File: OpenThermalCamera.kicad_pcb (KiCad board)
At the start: 2 copper layers, 26 x 20 mm, 18 parts, among them J1 Conn_ARM_JTAG_SWD_10, J2 USB_CONN, SW1 PB_Bootloader, U1 MLX90640, U2 TPS793333-EP, U3 STM32F042F6Px, U4 NUP2202

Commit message: Rev2
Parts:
- added D1: LED_Dual_ACAC, LED_SMD:LED_Cree-PLCC4_2x2mm_CW, B.Cu at (31.0, 30.7)
- added G1: , Symbol:OSHW-Logo2_7.3x6mm_SilkScreen, F.Cu at (31.2, 43.4)
- added R4: 5k1, Resistor_SMD:R_0805_2012Metric_Pad1.15x1.40mm_HandSolder, B.Cu at (34.4, 33.2)
- added R5: 10R, Resistor_SMD:R_0805_2012Metric_Pad1.15x1.40mm_HandSolder, F.Cu at (36.7, 43.9)
- added R6: 130R, Resistor_SMD:R_0805_2012Metric_Pad1.15x1.40mm_HandSolder, F.Cu at (36.7, 42.0)
- J2: value USB_CONN -> DX07P024AJ1R1500; footprint usb_b2b_connector:usb_b2b_connector -> lib_fp:DX07P024AJ1R1500
- R2, R3: value 2k2 -> 4k7
- SW1: footprint Button_Switch_SMD:SW_SPST_FSMSM -> Jumper:SolderJumper-2_P1.3mm_Open_RoundedPad1.0x1.5mm
- U1: footprint Package_TO_SOT_THT:TO-39-4_Window -> lib_fp:MLX90640
- moved SW1 20.3 mm to (49.7, 44.3)
- moved J2 4.70 mm to (40.4, 29.5), turned to 180 degrees
- moved U4 4.25 mm to (46.2, 33.4)
- moved R3 3.81 mm to (40.2, 36.6)
- moved C2 1.60 mm to (44.4, 43.7)
- moved U2 1.10 mm to (46.8, 43.6)
- moved C5 0.90 mm to (33.1, 36.7)
- moved C1 0.80 mm to (49.4, 43.7)
- moved C4 0.71 mm to (35.5, 36.6)
- moved C3 0.70 mm to (46.8, 40.2)
- moved C6 0.60 mm to (51.3, 43.7)
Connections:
- U3 pad 17: /USB_P -> /USB_N
- U3 pad 18: /USB_N -> /USB_P
- U3 pad 6: Net-(U3-Pad6) -> /BLUE_LED
- U3 pad 7: Net-(U3-Pad7) -> /RED_LED
- U4 pad 1: /USB_N -> /USB_P
- U4 pad 6: /USB_P -> /USB_N
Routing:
- net /BOOT0: track 39.2 -> 6.43 mm
- net Net-(D1-Pad1): track 0.00 -> 17.4 mm, vias 0 -> 1
- net Net-(D1-Pad4): track 0.00 -> 14.7 mm, vias 0 -> 1
- net +5V: track 33.2 -> 46.0 mm, vias 0 -> 3
- net Net-(J2-PadA5): track 0.00 -> 10.3 mm, vias 0 -> 1
- net /BLUE_LED: track 0.00 -> 8.67 mm, vias 0 -> 1
- net /RED_LED: track 0.00 -> 8.16 mm, vias 0 -> 1
- net GND: track 91.9 -> 84.6 mm, vias 11 -> 12
- net +3V3: track 62.5 -> 56.2 mm
- net /USB_P: track 32.5 -> 26.5 mm
- net /USB_N: track 31.4 -> 27.9 mm
- net /I2C_SDA: track 13.3 -> 12.3 mm, vias 2 -> 1
- net /I2C_SCL: track 8.79 -> 9.21 mm, vias 2 -> 1
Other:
- board size 26 x 20 mm -> 26 x 20.6 mm
- board text added: "OTC Rev2"

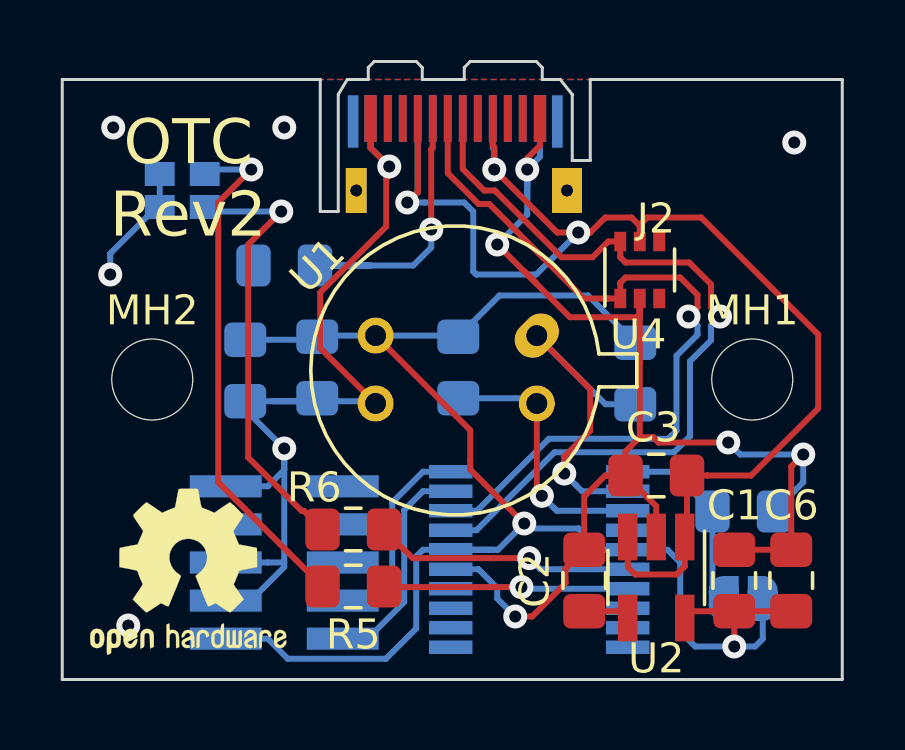
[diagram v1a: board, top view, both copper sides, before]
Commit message: Rev3: fixed MLX90640 footprint
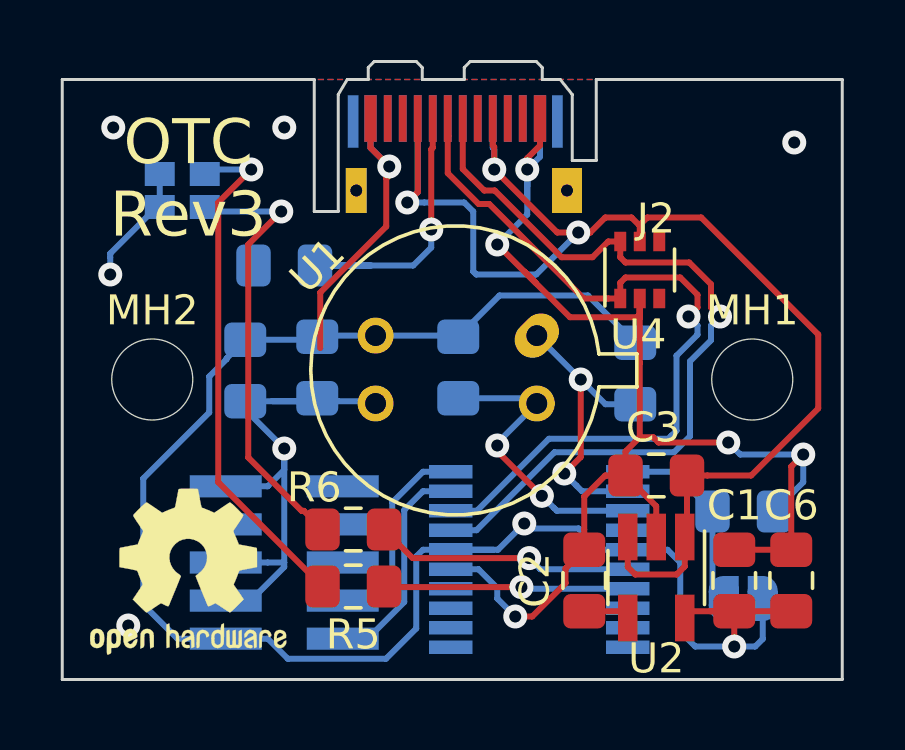
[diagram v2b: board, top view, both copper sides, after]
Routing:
- net +3V3: track 56.2 -> 60.8 mm
- net GND: track 84.6 -> 82.0 mm
- net /I2C_SDA: track 12.3 -> 9.95 mm, vias 1 -> 2
- net /I2C_SCL: track 9.21 -> 10.5 mm, vias 1 -> 2
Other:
- outline, holes or cut-outs redrawn
- board text added: "OTC Rev3"
- board text removed: "OTC Rev2"

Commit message: Fixed USB Type-C edge cuts
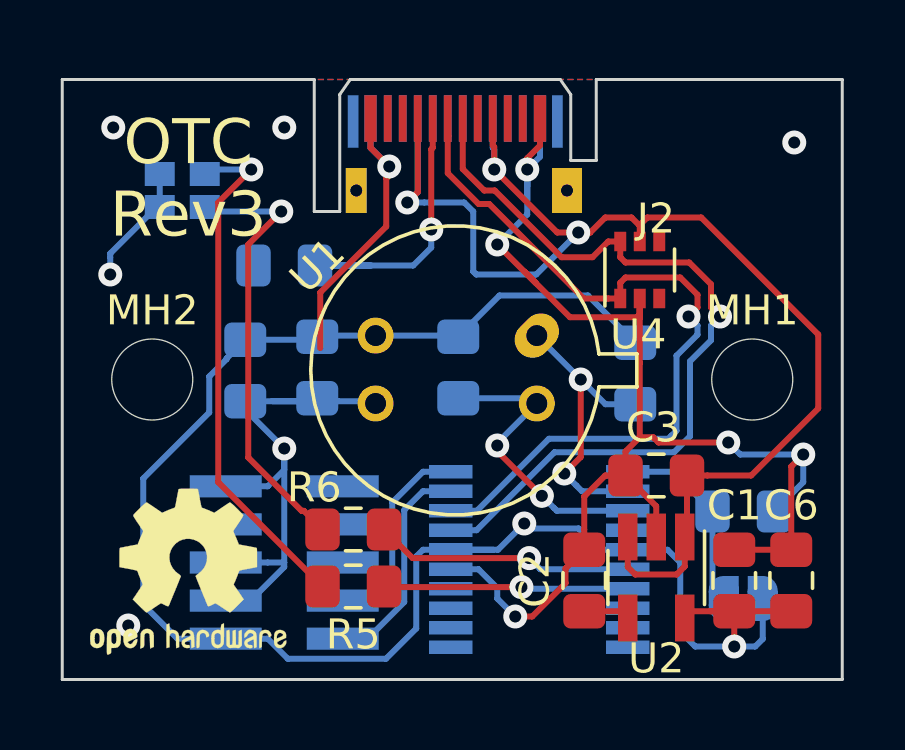
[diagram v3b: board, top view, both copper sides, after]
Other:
- board size 26 x 20.6 mm -> 26 x 20 mm
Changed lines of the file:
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@@
   (general
     (thickness 0.8)
-    (drawings 28)
+    (drawings 16)
     (tracks 299)
     (zones 0)
@@
       (xy -0.113933 -2.757629) (xy -0.013056 -2.757714) (xy 0 -2.757714) (xy 0.10391 -2.757652)) (layer F.SilkS) (width 0.01))
   )
+  (gr_line (start 43.95 27.5) (end 43.6 27) (layer Edge.Cuts) (width 0.1))
+  (gr_line (start 36.25 27.5) (end 36.6 27) (layer Edge.Cuts) (width 0.1))
   (gr_text "OTC\nRev3" (at 31.2 30.3) (layer F.SilkS)
     (effects (font (size 1.5 1.5) (thickness 0.3)))
   )
-  (gr_line (start 44 29.7) (end 44.8 29.7) (layer Edge.Cuts) (width 0.1))
-  (gr_line (start 44 27.5) (end 44 29.7) (layer Edge.Cuts) (width 0.1))
-  (gr_line (start 43.6 27) (end 44 27.5) (layer Edge.Cuts) (width 0.1))
-  (gr_line (start 43 27) (end 43.6 27) (layer Edge.Cuts) (width 0.1))
-  (gr_line (start 43 26.6) (end 43 27) (layer Edge.Cuts) (width 0.1))
-  (gr_line (start 42.8 26.4) (end 43 26.6) (layer Edge.Cuts) (width 0.1))
-  (gr_line (start 40.6 26.4) (end 42.8 26.4) (layer Edge.Cuts) (width 0.1))
-  (gr_line (start 40.4 26.6) (end 40.6 26.4) (layer Edge.Cuts) (width 0.1))
-  (gr_line (start 40.4 27) (end 40.4 26.6) (layer Edge.Cuts) (width 0.1))
-  (gr_line (start 39 27) (end 40.4 27) (layer Edge.Cuts) (width 0.1))
-  (gr_line (start 39 26.6) (end 39 27) (layer Edge.Cuts) (width 0.1))
-  (gr_line (start 38.8 26.4) (end 39 26.6) (layer Edge.Cuts) (width 0.1))
-  (gr_line (start 37.4 26.4) (end 38.8 26.4) (layer Edge.Cuts) (width 0.1))
-  (gr_line (start 37.2 26.6) (end 37.4 26.4) (layer Edge.Cuts) (width 0.1))
-  (gr_line (start 37.2 27) (end 37.2 26.6) (layer Edge.Cuts) (width 0.1))
-  (gr_line (start 36.5 27) (end 37.2 27) (layer Edge.Cuts) (width 0.1))
-  (gr_line (start 36.2 27.5) (end 36.5 27) (layer Edge.Cuts) (width 0.1))
-  (gr_line (start 36.2 31.4) (end 36.2 27.5) (layer Edge.Cuts) (width 0.1))
-  (gr_line (start 35.4 31.4) (end 36.2 31.4) (layer Edge.Cuts) (width 0.1))
+  (gr_line (start 43.95 29.7) (end 44.8 29.7) (layer Edge.Cuts) (width 0.1))
+  (gr_line (start 43.95 27.5) (end 43.95 29.7) (layer Edge.Cuts) (width 0.1))
+  (gr_line (start 36.6 27) (end 43.6 27) (layer Edge.Cuts) (width 0.1))
+  (gr_line (start 36.25 31.4) (end 36.25 27.5) (layer Edge.Cuts) (width 0.1))
+  (gr_line (start 35.4 31.4) (end 36.25 31.4) (layer Edge.Cuts) (width 0.1))
   (gr_line (start 44.8 27) (end 44.8 29.7) (layer Edge.Cuts) (width 0.1))
   (gr_line (start 35.4 31.4) (end 35.4 27) (layer Edge.Cuts) (width 0.1))
